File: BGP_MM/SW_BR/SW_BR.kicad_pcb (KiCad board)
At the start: 2 copper layers, 12 x 13 mm, 2 parts, among them P1 CONN_01X03, P2 CONN_01X02

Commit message: MM Gerbers, BASS pot fixup
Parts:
- P1: moved to F.Cu
- P2: moved to B.Cu
- moved P1 9.40 mm to (141.6, 111.2), turned to 270 degrees
- moved P2 2.00 mm to (147.8, 107.5), turned to 90 degrees

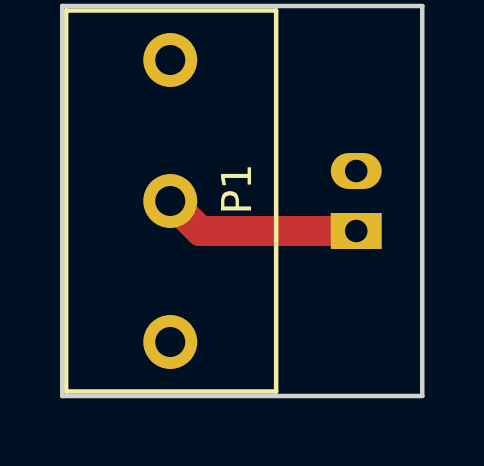
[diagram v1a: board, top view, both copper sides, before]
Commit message: MM Gerbers Finished, Mid Stack Ammended J0
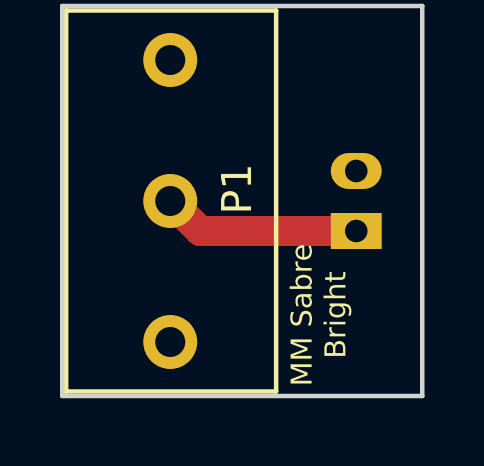
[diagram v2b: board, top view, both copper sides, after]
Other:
- board text added: "MM Sabre Bright"
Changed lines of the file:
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@@
-(kicad_pcb (version 4) (host pcbnew 4.0.4-1.fc24-product)
+(kicad_pcb (version 4) (host pcbnew 4.0.7)
   (general
     (links 3)
     (no_connects 0)
-    (area 135.905 99.774999 150.125001 113.225001)
+    (area 135.905 99.774999 150.225001 113.225001)
     (thickness 1.6)
-    (drawings 4)
+    (drawings 5)
     (tracks 2)
     (zones 0)
@@
     (pad_to_mask_clearance 0.2)
     (aux_axis_origin 0 0)
-    (visible_elements FFFFFF7F)
+    (visible_elements 7FFFFFFF)
     (pcbplotparams
       (layerselection 0x010fc_80000001)
@@
     )
   )
+  (gr_text "MM Sabre\nBright" (at 146.55 110.3 90) (layer F.SilkS)
+    (effects (font (size 0.7 0.7) (thickness 0.175)))
+  )
   (gr_line (start 138 113) (end 138 100) (layer Edge.Cuts) (width 0.15))

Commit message: MM Refactoring
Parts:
- added P3: CONN_01X02, Connectors_JST:JST_PH_B2B-PH-K_02x2.00mm_Straight, B.Cu at (151.8, 110.0)
- added SW1: SW_DPDT, LIBS:NKK_DPDT, F.Cu at (146.1, 101.6)
- P1: value CONN_01X03 -> CONN_01X04; footprint LIBS:NKK_SPDT -> Connectors_JST:JST_PH_B4B-PH-K_04x2.00mm_Straight; moved to B.Cu
- moved P2 5.37 mm to (151.8, 104.0)
- moved P1 2.86 mm to (140.7, 113.9), turned to 0 degrees
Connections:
- P1 pad 2: Net-(P1-Pad2) -> /ACT_I
- P1 pad 3: Earth -> /SEL_I
- P2 pad 1: Net-(P1-Pad2) -> /SEL_I
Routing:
- net /SEL_I: track 0.00 -> 19.3 mm
- net /VOL_O: track 0.00 -> 15.0 mm
- net /ACT_I: track 0.00 -> 12.9 mm
- net /BR_I: track 0.00 -> 8.66 mm
- net Net-(P1-Pad2): track 6.61 -> 0.00 mm
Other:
- board size 12 x 13 mm -> 16 x 16 mm
- net class Default: clearance 0.2 -> 0.3; trace_width 0.25 -> 0.4
- rule trace_clearance: 0.2 -> 0.3
- board text removed: "MM Sabre Bright"

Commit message: MM Refactoring
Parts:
- removed P1: CONN_01X04, Connectors_JST:JST_PH_B4B-PH-K_04x2.00mm_Straight
- removed P2, P3: CONN_01X02, Connectors_JST:JST_PH_B2B-PH-K_02x2.00mm_Straight
- added J1: Conn_01x05_Male, Pin_Headers:Pin_Header_Straight_1x05_Pitch2.54mm, F.Cu at (153.9, 101.6)
- added J2: Conn_01x05_Male, Pin_Headers:Pin_Header_Straight_1x05_Pitch2.54mm, F.Cu at (151.0, 101.6)
- added J3: Conn_01x05_Male, Pin_Headers:Pin_Header_Straight_1x05_Pitch2.54mm, F.Cu at (156.9, 101.6)
- added J4: Conn_01x02, LIBS:TerminalBlock_Phoenix_MPT-2.54mm_2pol, F.Cu at (148.4, 116.7)
- added J5: Conn_01x03, LIBS:TerminalBlock_Phoenix_MPT-2.54mm_3pol, F.Cu at (139.7, 116.7)
- SW1: moved to B.Cu
- moved SW1 10.0 mm to (146.1, 111.6), turned to 270 degrees
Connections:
- SW1 pad 1: Net-(SW1-Pad1) -> Earth
- SW1 pad 2: /BR_I -> /BR
- SW1 pad 3: Earth -> Net-(SW1-Pad3)
- SW1 pad 4: /ACT_I -> /MID
- SW1 pad 5: /VOL_O -> /VOL_I
- SW1 pad 6: /SEL_I -> /SEL
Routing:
- net /MID: track 0.00 -> 21.9 mm
- net /SEL: track 0.00 -> 20.8 mm
- net /SEL_I: track 19.3 -> 0.00 mm
- net /ACT_I: track 12.9 -> 0.00 mm
- net VCC: track 0.00 -> 12.8 mm
- net /VOL_I: track 0.00 -> 11.3 mm
- net /BR: track 0.00 -> 8.78 mm
- net /BR_I: track 8.66 -> 0.00 mm
- net /VOL_O: track 15.0 -> 19.7 mm
- net Net-(J4-Pad1): track 0.00 -> 3.60 mm
- net /ACT: track 0.00 -> 2.95 mm
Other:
- board size 16 x 16 mm -> 20.5 x 20 mm
- net class Default: clearance 0.3 -> 0.26; trace_width 0.4 -> 0.3
- rule trace_clearance: 0.3 -> 0.26

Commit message: MM PCB comments
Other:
- board text added: "B+"
- board text added: "B-"
- board text added: "RING"
- board text added: "SLV"
- board text added: "TIP"
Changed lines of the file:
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@@
     (area 137.564999 99.514999 161.81 122.09588)
     (thickness 1.6)
-    (drawings 8)
+    (drawings 13)
     (tracks 36)
     (zones 0)
@@
     )
   )
+  (gr_text SLV (at 139.7 118.6) (layer B.SilkS)
+    (effects (font (size 0.6 0.6) (thickness 0.15)) (justify mirror))
+  )
+  (gr_text TIP (at 142.2 118.6) (layer B.SilkS)
+    (effects (font (size 0.6 0.6) (thickness 0.15)) (justify mirror))
+  )
+  (gr_text RING (at 144.8 118.6) (layer B.SilkS)
+    (effects (font (size 0.6 0.6) (thickness 0.15)) (justify mirror))
+  )
+  (gr_text B+ (at 150.9 118.6) (layer B.SilkS)
+    (effects (font (size 0.6 0.6) (thickness 0.15)) (justify mirror))
+  )
+  (gr_text B- (at 148.4 118.6) (layer B.SilkS)
+    (effects (font (size 0.6 0.6) (thickness 0.15)) (justify mirror))
+  )
   (gr_line (start 138.3 119.7) (end 138.3 100.3) (layer Margin) (width 0.2))
